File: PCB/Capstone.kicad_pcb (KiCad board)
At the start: 4 copper layers, 87.6 x 68.6 mm, 236 parts, among them J1 S2B-PH-SM4-TB, J10 DNP, J11 DNP, J12 DNP, J2 TRANSDUCER, J3 DNP, J4 PH1-08-UA, J5 DNP, J6 DNP, J7 DNP, J8 PH1-08-UA, J9 DNP, Q1 SSM6K361NU, SW1 SW_Push, SW2 SW_Push, SW3 SW_Push, U1 TPS63031, U10 AP2204K-ADJ, U11 LM3478, U12 10CL010, U13 ECS-5032MV, U14 TSX9291, U15 LTC6090-5, U16 AD5450, U17 ADA4522-1, U18 MAX5394L, U19 MAX5394L, U2 TCR2EF25, U20 MAX11116, U21 TLV3544, U22 MCP6L1, U3 TPS62262, U4 BMD-360, U5 MIC841N, U6 ENS210, U7 W25Q80DV, U8 LIS2DE12, U9 LMR62421

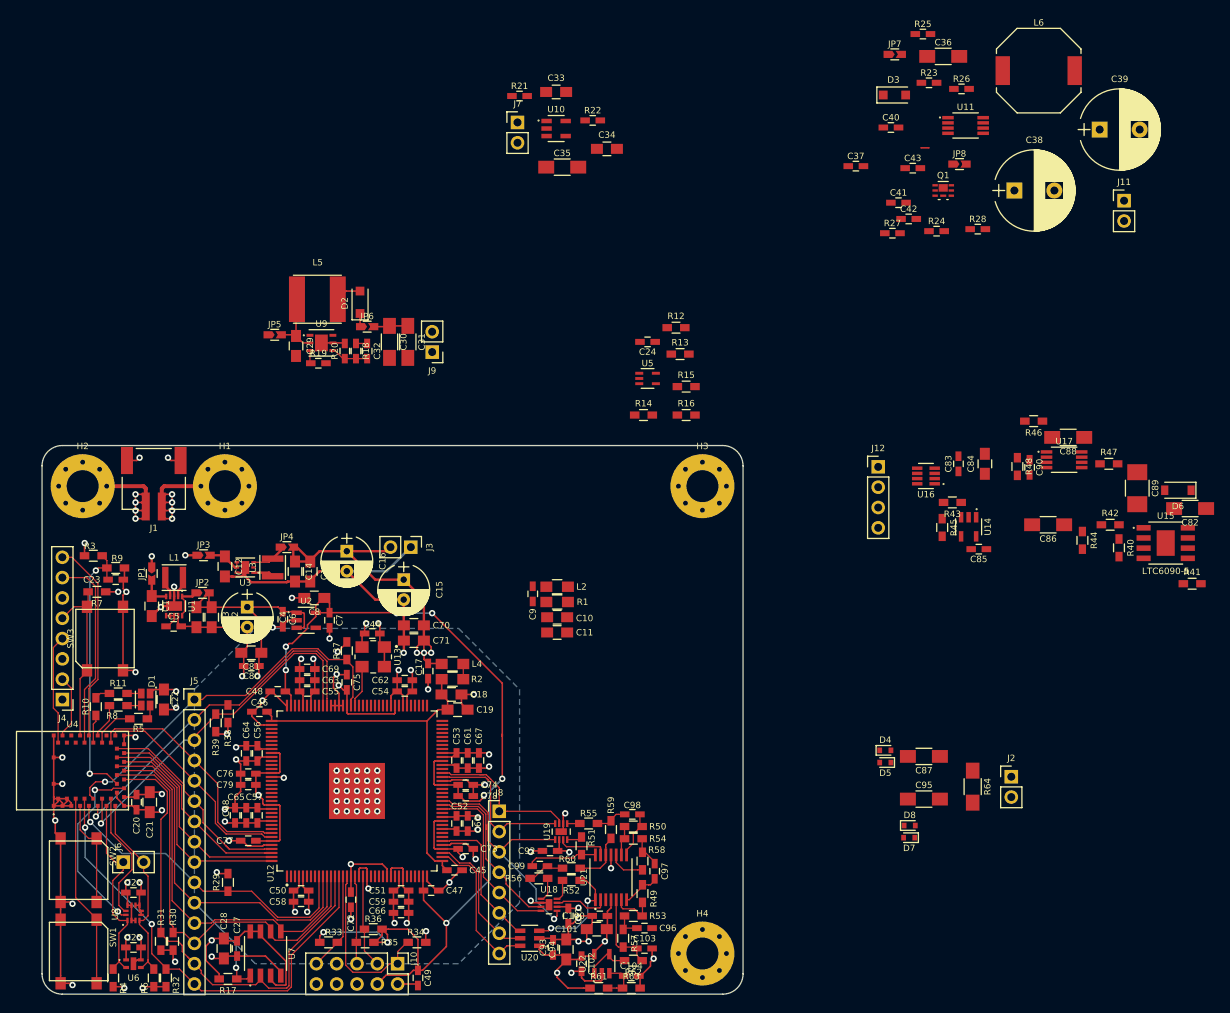
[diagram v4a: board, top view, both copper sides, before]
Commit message: Complete preliminary layout, add U of M logo for bottom silkscreen
Still need to run DRC and fix issues
Still need to fix top silkscreen so references are actually readable
Still need to fix bottom silkscreen to show group names
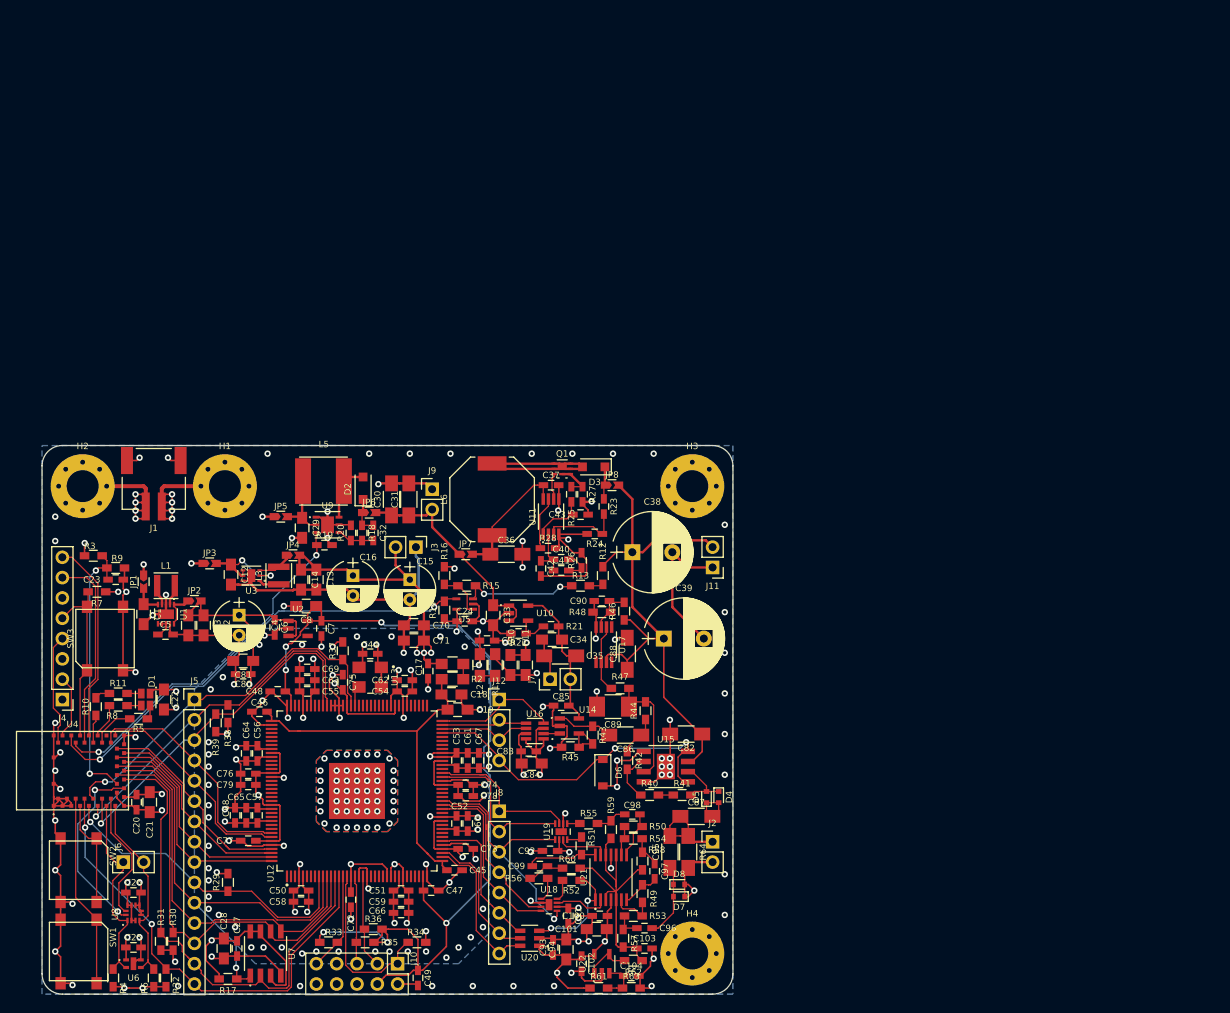
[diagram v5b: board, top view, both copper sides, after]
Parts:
- added Ref**: Val**, Parts:UofM, B.Cu at (157.7, 61.5)
- moved L6 86.8 mm to (142.6, 102.0), turned to 90 degrees
- moved C39 83.8 mm to (164.1, 119.4)
- moved C36 82.8 mm to (144.4, 108.8)
- moved JP7 82.3 mm to (139.3, 108.8)
- moved D6 80.1 mm to (156.5, 136.1), turned to 270 degrees
- moved R26 75.7 mm to (153.8, 109.6), turned to 90 degrees
- moved R25 72.4 mm to (152.5, 101.3), turned to 270 degrees
- moved U11 71.2 mm to (150.0, 104.1), turned to 90 degrees
- moved C89 71.0 mm to (157.7, 127.9), turned to 180 degrees
- moved J7 69.7 mm to (149.9, 124.5), turned to 90 degrees
- moved C82 69.0 mm to (166.9, 131.3)
- moved R41 69.0 mm to (166.4, 138.9)
- moved J11 68.9 mm to (170.2, 110.5), turned to 180 degrees
- moved U15 68.4 mm to (164.3, 135.4)
- moved C84 67.9 mm to (147.6, 135.0), turned to 180 degrees
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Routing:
- net GND: track 339.1 -> 477.1 mm, vias 81 -> 173
- net +50V: track 0.00 -> 70.2 mm
- net /Microcontroller/HV-OK: track 0.00 -> 58.8 mm, vias 0 -> 2
- net HV-ENABLE: track 1.63 -> 45.0 mm, vias 0 -> 2
- net TRANSMIT-ENABLE: track 0.00 -> 41.8 mm, vias 0 -> 2
- net Net-(D3-Pad2): track 0.00 -> 23.7 mm
- net +12V: track 4.32 -> 27.7 mm
- net +10V: track 0.00 -> 19.4 mm
- net GNDA-50V: track 0.00 -> 18.3 mm
- net +3V3-LN: track 29.0 -> 47.0 mm, vias 4 -> 6
- net Net-(C36-Pad1): track 0.00 -> 16.1 mm
- net DAC-~CS: track 0.00 -> 15.8 mm
- net /Transmit/MIDRAIL: track 0.00 -> 14.9 mm
- net Net-(R13-Pad2): track 0.00 -> 14.7 mm, vias 0 -> 2
- net /Receive/MIDRAIL: track 21.6 -> 36.0 mm
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- added copper zone on B.Cu, net GND
- added copper zone on F.Cu, net GND
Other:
- board size 87.6 x 68.6 mm -> 86.4 x 68.6 mm
- board text added: "ECE Capstone group G07"

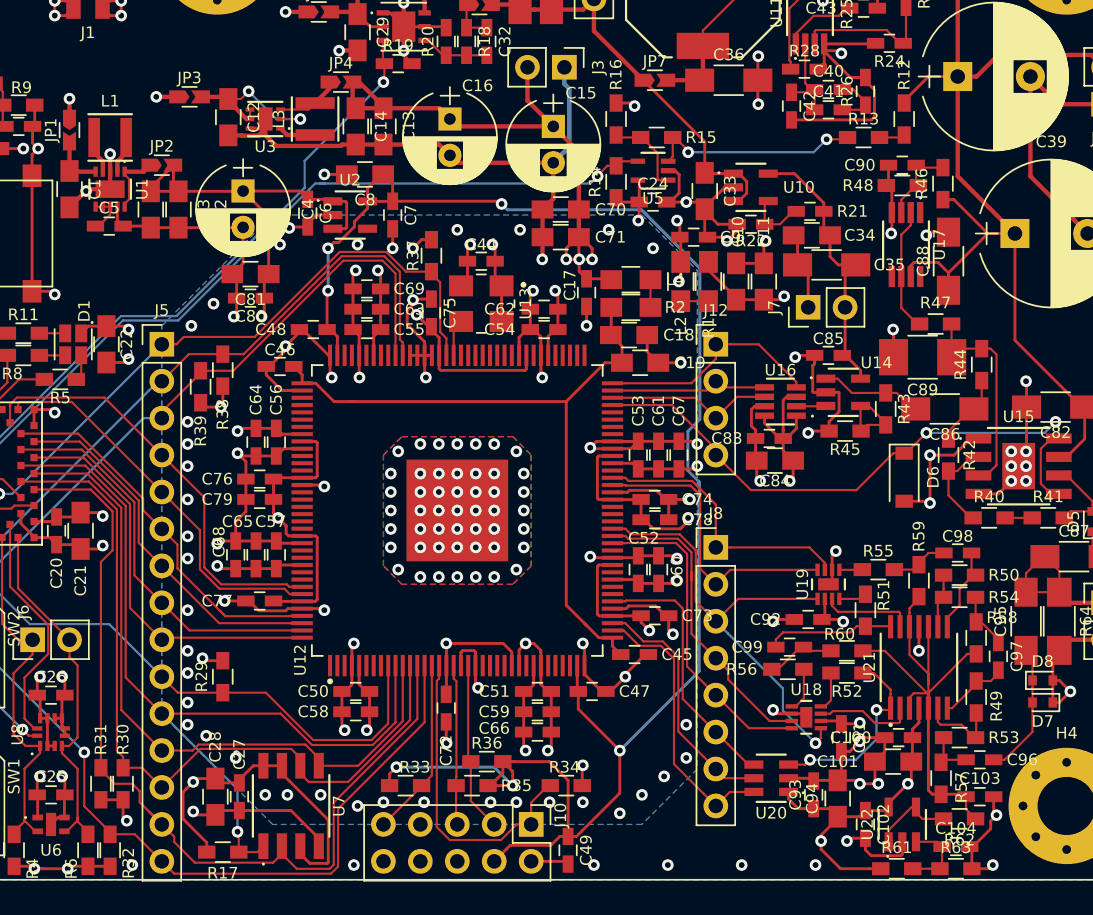
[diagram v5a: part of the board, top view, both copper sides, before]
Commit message: Fix DRC errors, fix 3D models for all important parts
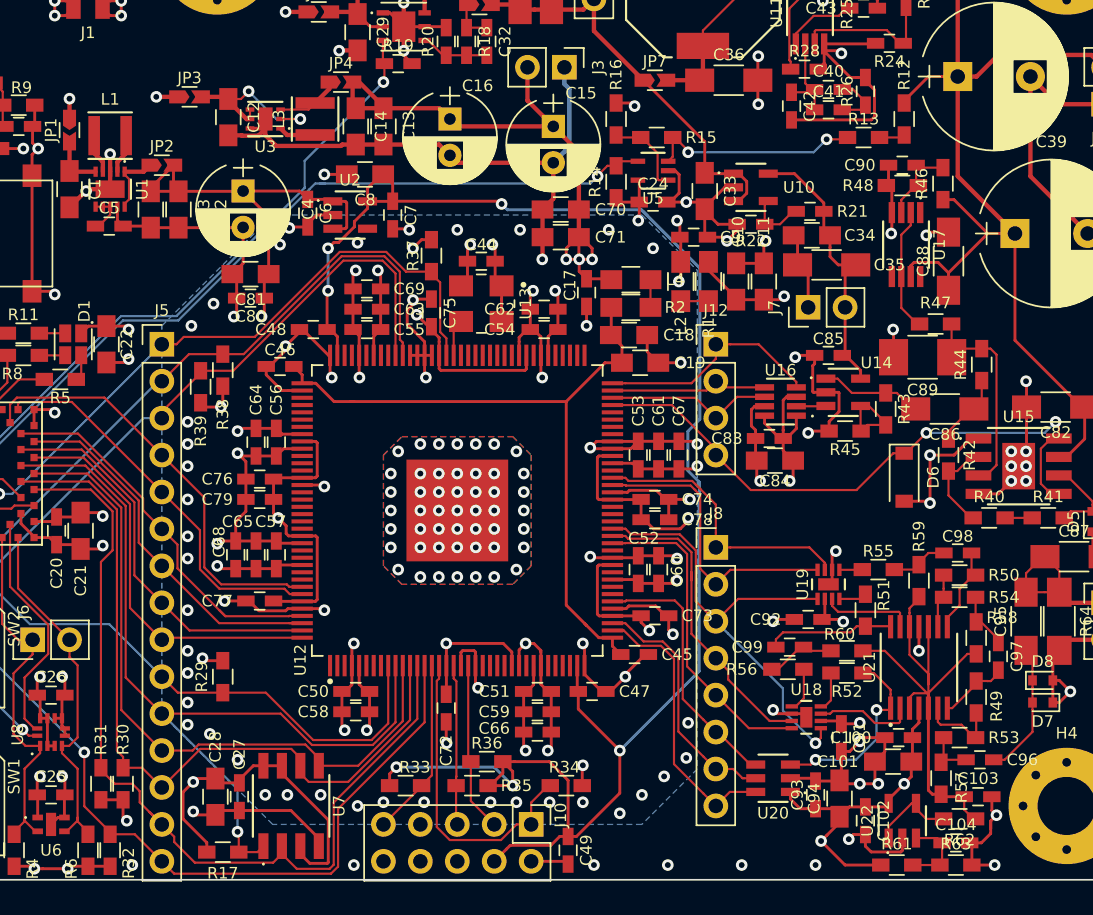
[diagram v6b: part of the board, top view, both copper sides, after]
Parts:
- moved C102 0.25 mm to (153.8, 159.8)
- moved C104 0.25 mm to (160.0, 161.3)
- moved R61 0.25 mm to (156.0, 162.8)
- moved R63 0.25 mm to (160.0, 162.8)
- moved U22 0.25 mm to (156.3, 159.8)
- moved C94 0.13 mm to (152.0, 158.2)
- moved U20 0.13 mm to (147.4, 156.8)
- moved L1 0.13 mm to (101.9, 112.6)
- moved C103 0.13 mm to (161.5, 158.1)
- moved C93 0.13 mm to (150.4, 158.0)
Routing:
- net +3V3-LN: track 47.0 -> 46.5 mm
- net GND: track 477.1 -> 477.6 mm

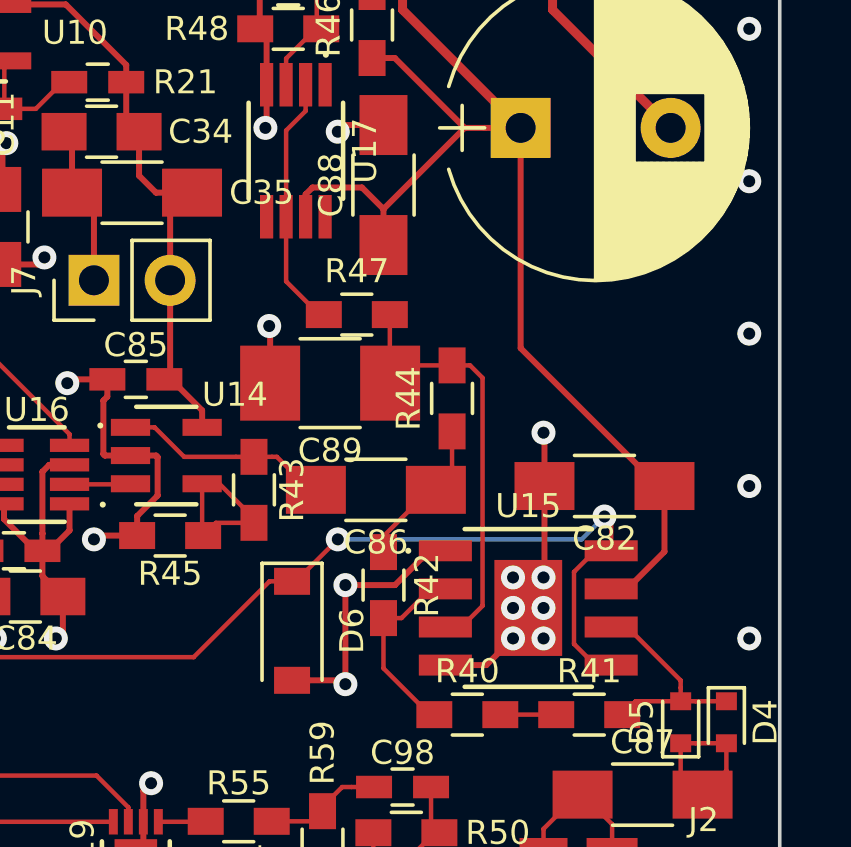
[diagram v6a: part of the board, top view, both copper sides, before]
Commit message: Give 50V traces extra clearance, add names to bottom silkscreen
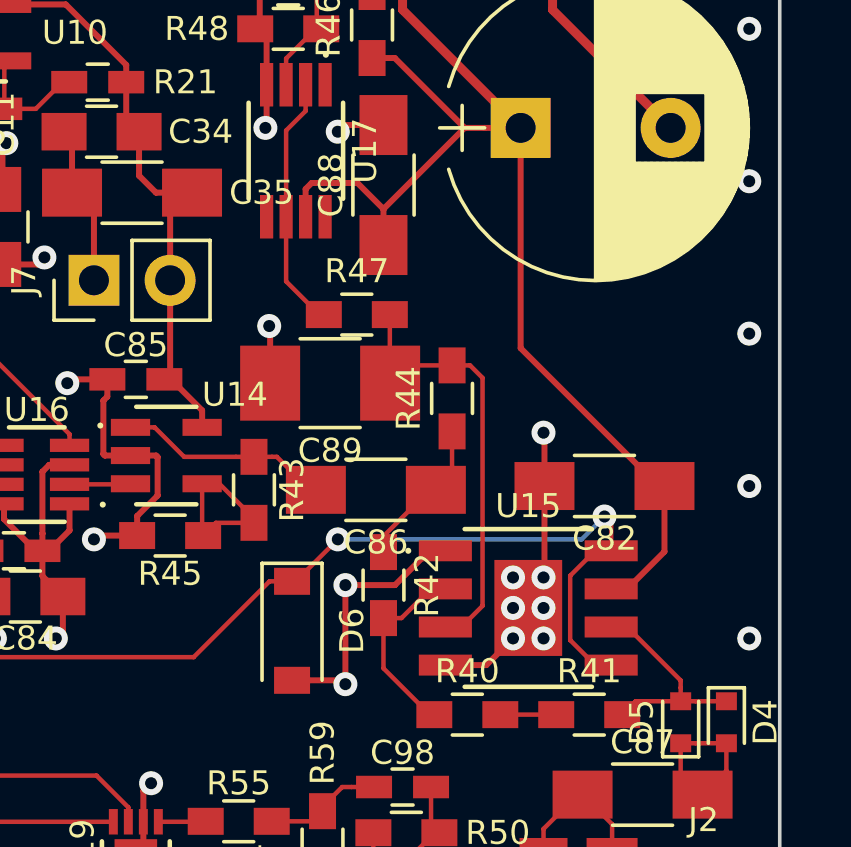
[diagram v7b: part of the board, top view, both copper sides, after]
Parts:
- removed Ref**: Val**, Parts:UofM
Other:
- net class Power50 added: clearance 0.3, trace_width 0.2, via_dia 0.8, via_drill 0.4
- net class Signal50 added: clearance 0.3, trace_width 0.15, via_dia 0.8, via_drill 0.4
- board text removed: "ECE Capstone group G07"

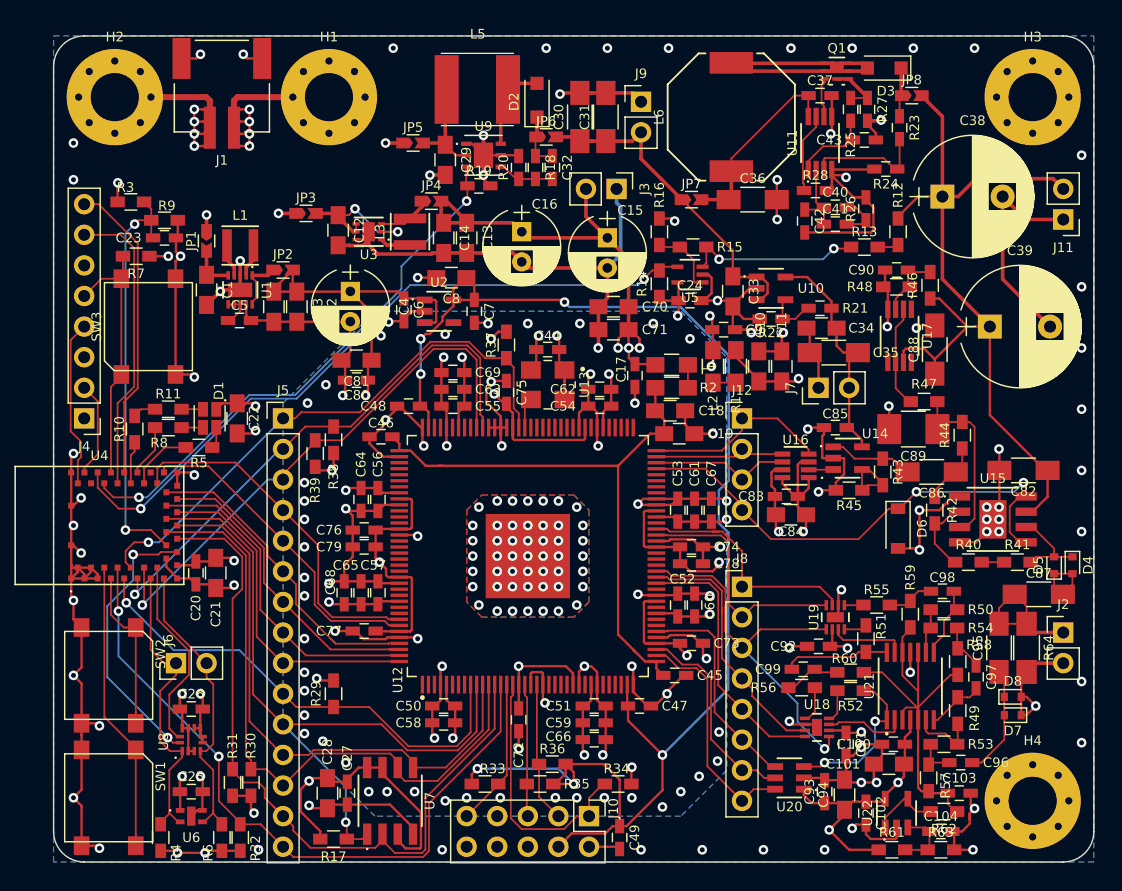
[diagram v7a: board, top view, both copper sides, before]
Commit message: Optimize routing on bottom of PCB for increased GND plane connectivity
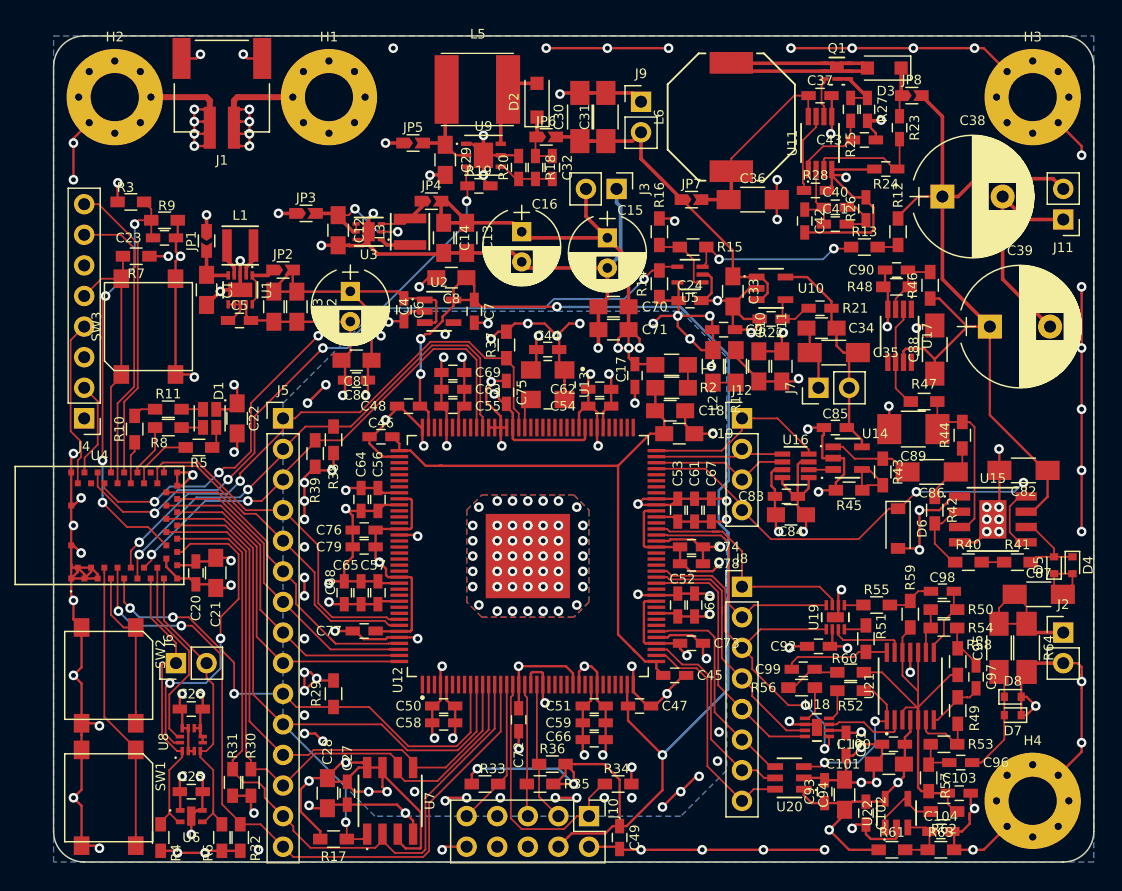
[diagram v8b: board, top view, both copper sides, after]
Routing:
- net GND: track 477.6 -> 576.3 mm, vias 173 -> 177
- net +3V3: track 165.0 -> 213.7 mm
- net FPGA-CRC_ERROR: track 46.1 -> 41.7 mm, vias 1 -> 2
- net /Microcontroller/ACC-INT1: track 23.1 -> 26.4 mm
- net FPGA-nCONFIG: track 58.8 -> 61.7 mm
- net HV-ENABLE: track 45.0 -> 47.7 mm, vias 2 -> 4
- net /Microcontroller/HV-OK: track 58.8 -> 60.5 mm, vias 2 -> 4
- net FPGA-nSTATUS: track 40.1 -> 41.6 mm, vias 1 -> 3
- net Net-(C23-Pad1): track 34.4 -> 35.8 mm, vias 2 -> 4
- net FPGA-INIT_DONE: track 44.9 -> 44.1 mm, vias 1 -> 2
- net VGA-SCK: track 34.0 -> 34.8 mm, vias 1 -> 2
- net FPGA-CONF_DONE: vias 1 -> 2
